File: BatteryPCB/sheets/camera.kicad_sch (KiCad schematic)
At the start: 3 parts, among them J3 RunCam Split 4

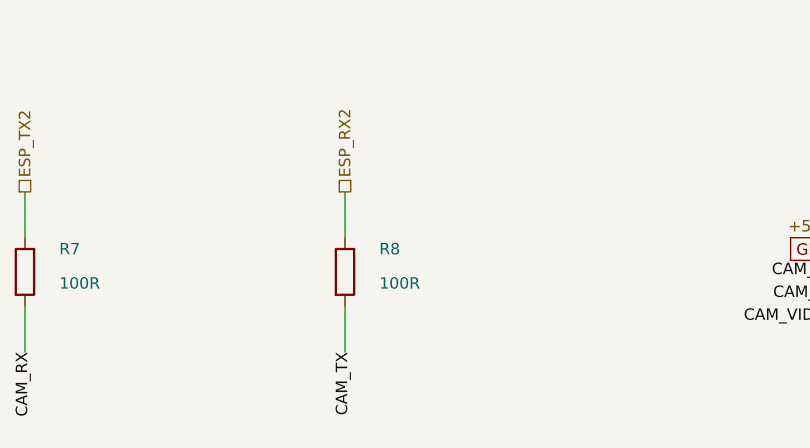
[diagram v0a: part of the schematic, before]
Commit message: Battery PCB v21: R8 1k camera-RX protection, separate drill files
- R8 (camera TX -> ESP32 RX) 100R -> 1k: protects GPIO16 if the
  RunCam's UART turns out to be 5 V.
- Separate PTH/NPTH drill files; tools/make_fab.sh rebuilds fab/.
- README: camera logic-level check, USB + board power is safe (DevKitC
  feeds 5V from USB through a Schottky).
ERC 0 errors, DRC 0 (strict, schematic parity), verify_A all pass.

Co-Authored-By: Claude Opus 5.5 <noreply@anthropic.com>
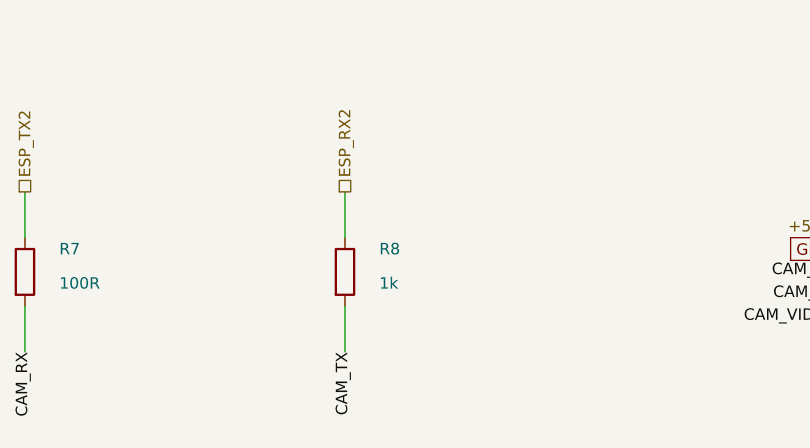
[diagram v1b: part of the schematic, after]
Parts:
- R8: value 100R -> 1k; MPN RC0603FR-07100RL -> RC0603FR-071KL
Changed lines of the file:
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@@
 			(effects (font (size 1.27 1.27)) (justify left))
 		)
-		(property "Value" "100R"
+		(property "Value" "1k"
 			(at 114.3 55.88 0)
 			(effects (font (size 1.27 1.27)) (justify left))
@@
 			(effects (font (size 1.27 1.27)) (hide yes))
 		)
-		(property "MPN" "RC0603FR-07100RL"
+		(property "MPN" "RC0603FR-071KL"
 			(at 110.49 54.61 0)
 			(effects (font (size 1.27 1.27)) (hide yes))
